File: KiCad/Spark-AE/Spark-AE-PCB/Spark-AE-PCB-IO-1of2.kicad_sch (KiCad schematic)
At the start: 21 parts, among them J3 Inputs, J4 Outputs, U4 MCP6002-xSN, U5 MCP6002-xSN

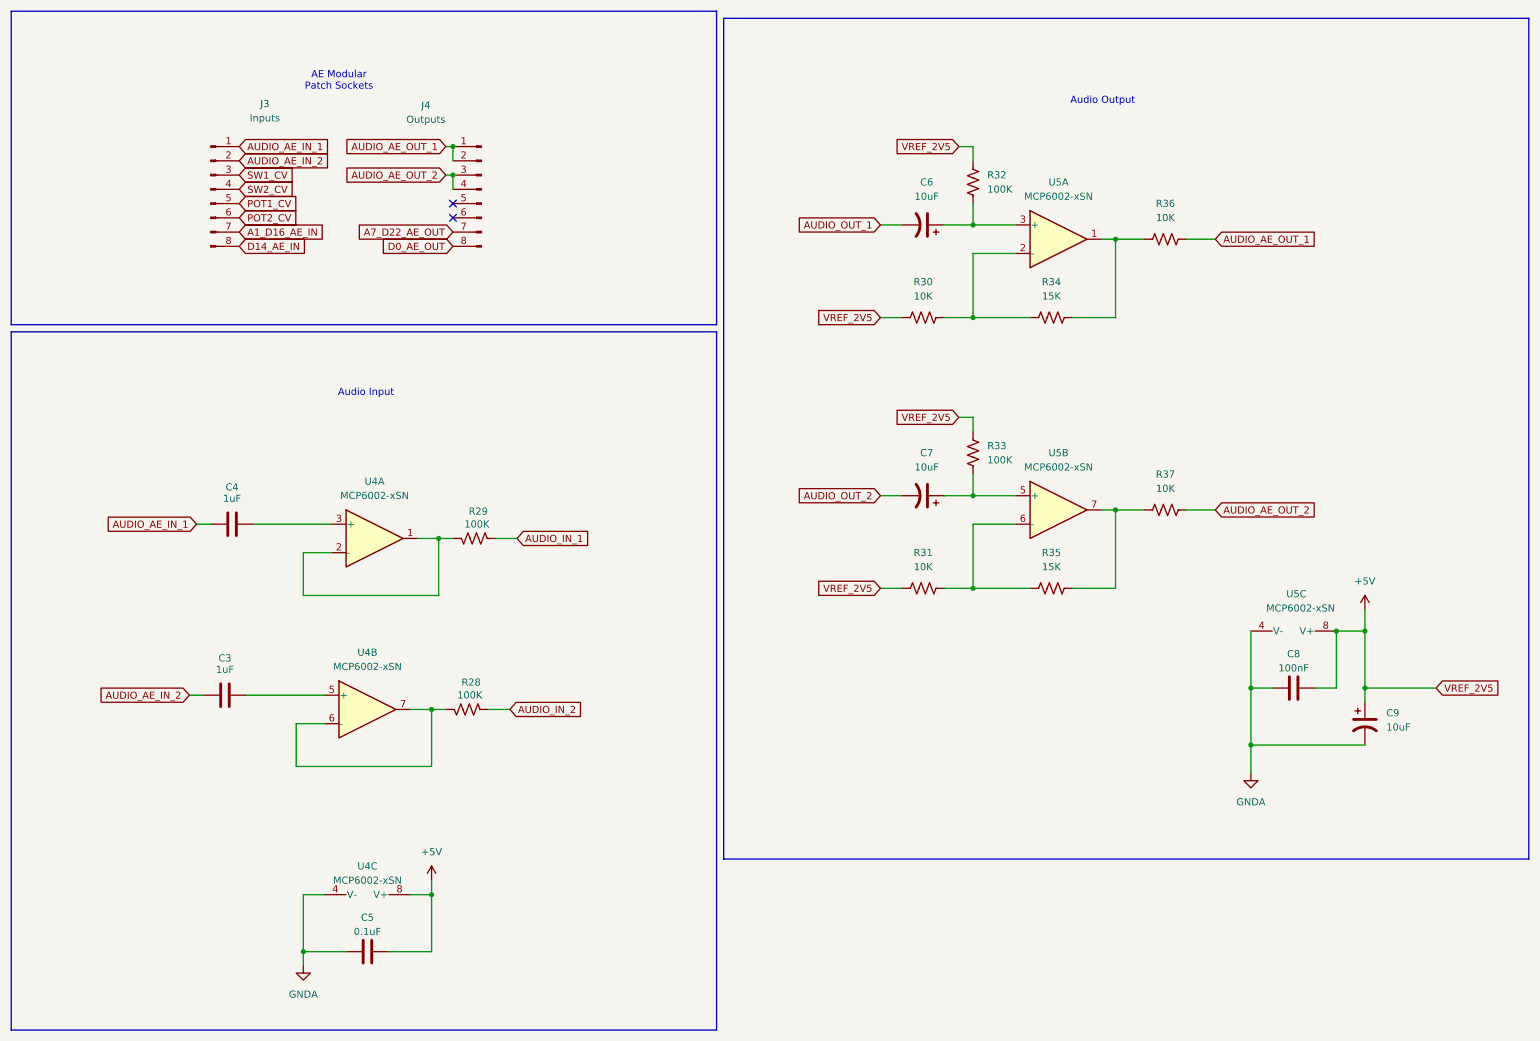
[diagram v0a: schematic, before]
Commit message: assigned footprints & sorted ratsnest
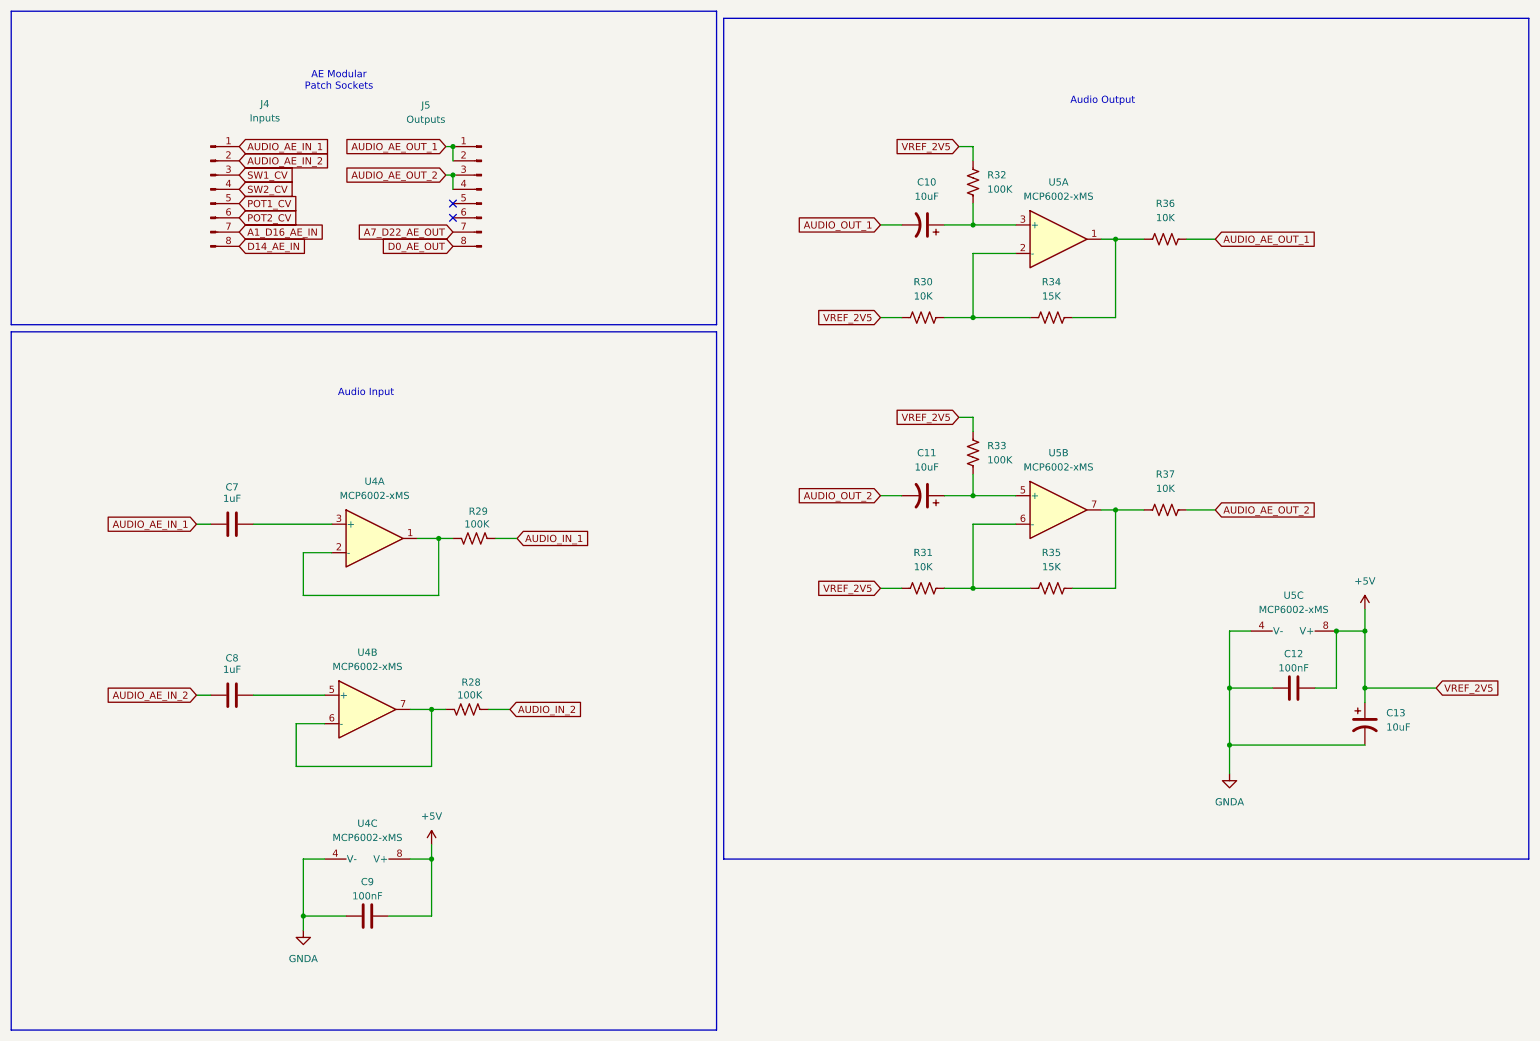
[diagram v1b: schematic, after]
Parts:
- removed U4, U5: MCP6002-xSN, symbol Amplifier_Operational:MCP6002-xSN
- added U4, U5: MCP6002-xMS, clectric-diy:Amplifier_Operational_Microchip_MCP6002T-I_MS, symbol Amplifier_Operational:MCP6002-xMS
- C10: renamed from C6; footprint (none) -> Capacitor_SMD:CP_Elec_4x5.4
- C11: renamed from C7; footprint (none) -> Capacitor_SMD:CP_Elec_4x5.4
- C12: renamed from C8; footprint (none) -> Capacitor_SMD:C_0603_1608Metric
- C13: renamed from C9; footprint (none) -> Capacitor_SMD:CP_Elec_4x5.4
- C7: renamed from C4; footprint Capacitor_THT:C_Rect_L7.2mm_W2.5mm_P5.00mm -> Capacitor_SMD:C_0603_1608Metric
- C8: renamed from C3; footprint Capacitor_THT:C_Rect_L7.2mm_W2.5mm_P5.00mm -> Capacitor_SMD:C_0603_1608Metric
- C9: renamed from C5; value 0.1uF -> 100nF; footprint (none) -> Capacitor_SMD:C_0603_1608Metric
- J4: renamed from J3; footprint (none) -> clectric-diy:Connector_PinSocket-1x08-P2.54mm-H8.5mm_Preci-Dip_801-87-008-10-005101
- J5: renamed from J4; footprint (none) -> clectric-diy:Connector_PinSocket-1x08-P2.54mm-H8.5mm_Preci-Dip_801-87-008-10-005101
- R28, R29, R30, R31, R32, R33, R34, R35, R36, R37: footprint (none) -> Resistor_SMD:R_0603_1608Metric
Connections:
- net +5V: now also U4.8 (V+), U5.8 (V+)
- net GNDA: now also U4.4 (V-), U5.4 (V-)
- net at R28.1: now also U4.6 (-), U4.7
- net at R29.1: now also U4.1, U4.2 (-)
- net at C7.2: now also U4.3 (+)
- net at R30.2, R34.1: now also U5.2 (-)
- net at R34.2, R36.1: now also U5.1
- net at R31.2, R35.1: now also U5.6 (-)
- net at R35.2, R37.1: now also U5.7
- net at C10.1, R32.2: now also U5.3 (+)
- net at C11.1, R33.2: now also U5.5 (+)
- net at C8.2: now also U4.5 (+)
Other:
- moved on the sheet: C8, C9

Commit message: schematic 100% complete. pcb layout around 50% complete.
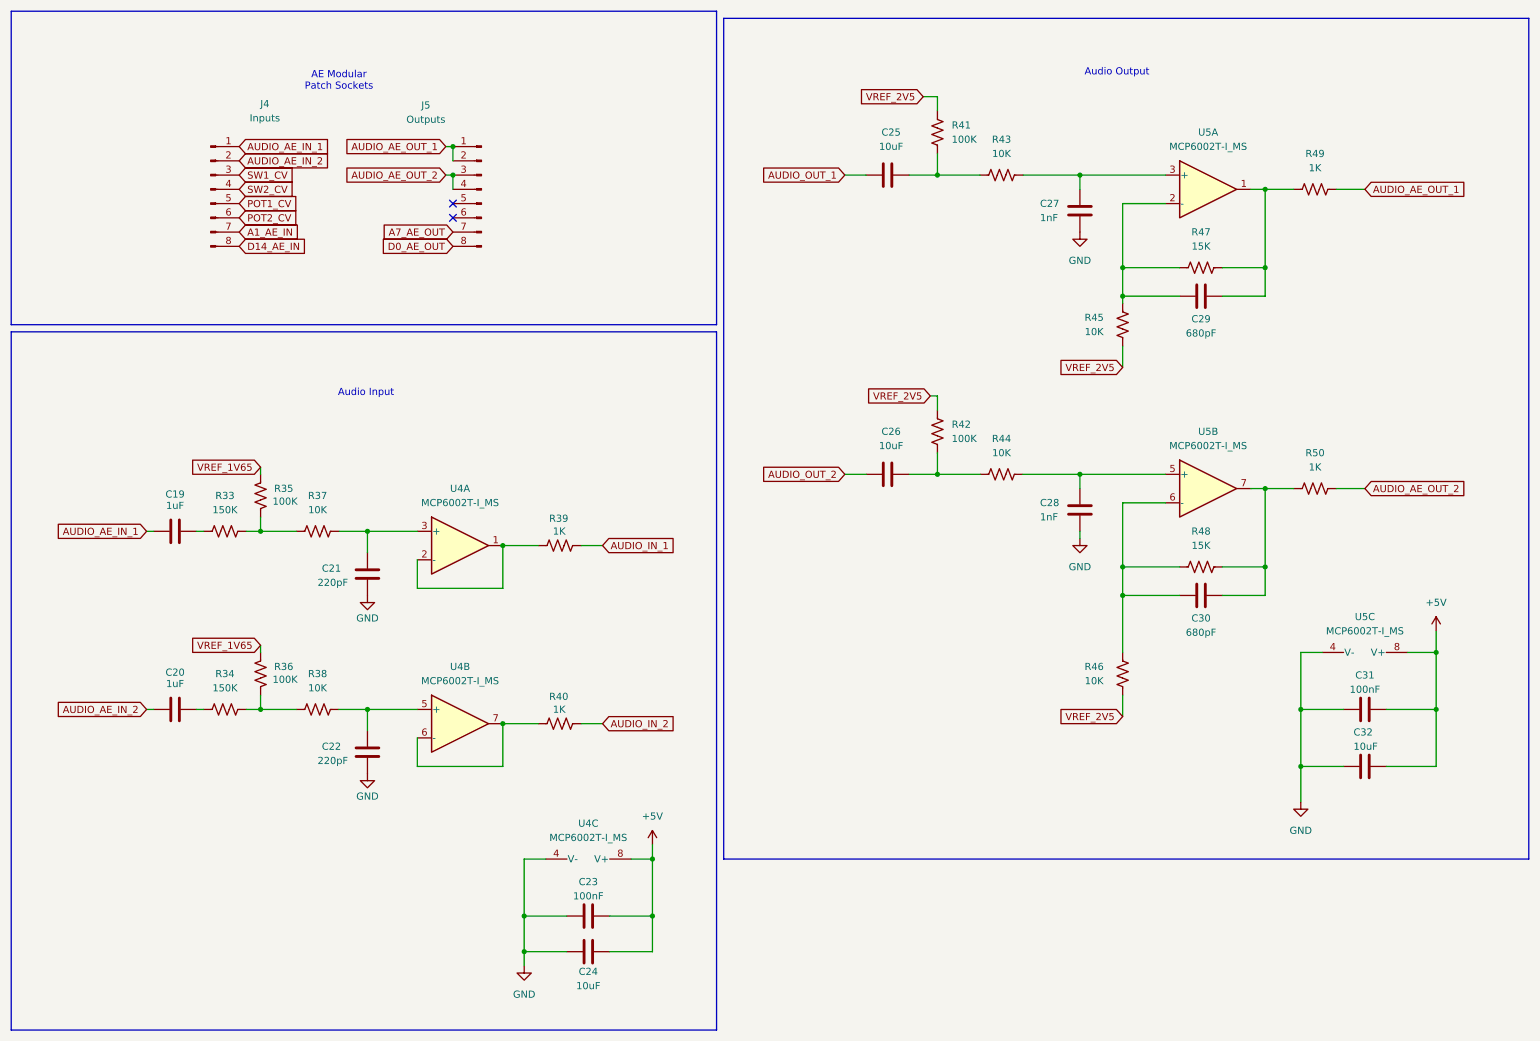
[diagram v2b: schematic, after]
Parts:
- removed C7: 1uF, Capacitor_SMD:C_0603_1608Metric, symbol Device:C
- removed R29: 100K, Resistor_SMD:R_0603_1608Metric, symbol Device:R_US
- added C19: 1uF, Capacitor_SMD:C_0603_1608Metric, symbol Device:C
- added C21, C22: 220pF, Capacitor_SMD:C_0603_1608Metric, symbol Device:C
- added C24: 10uF, Capacitor_SMD:C_0603_1608Metric, symbol Device:C
- added C27, C28: 1nF, Capacitor_SMD:C_0603_1608Metric, symbol Device:C
- added C29, C30: 680pF, Capacitor_SMD:C_0603_1608Metric, symbol Device:C
- added R33, R34: 150K, Resistor_SMD:R_0603_1608Metric, symbol Device:R_US
- added R35, R36: 100K, Resistor_SMD:R_0603_1608Metric, symbol Device:R_US
- added R37, R38, R43, R44: 10K, Resistor_SMD:R_0603_1608Metric, symbol Device:R_US
- added R39: 1K, Resistor_SMD:R_0603_1608Metric, symbol Device:R_US
- C25: renamed from C10; footprint Capacitor_SMD:CP_Elec_4x5.4 -> Capacitor_SMD:C_0603_1608Metric; symbol Device:C_Polarized_US -> Device:C
- C26: renamed from C11; footprint Capacitor_SMD:CP_Elec_4x5.4 -> Capacitor_SMD:C_0603_1608Metric; symbol Device:C_Polarized_US -> Device:C
- C32: renamed from C13; footprint Capacitor_SMD:CP_Elec_4x5.4 -> Capacitor_SMD:C_0603_1608Metric; symbol Device:C_Polarized_US -> Device:C
- R40: renamed from R28; value 100K -> 1K
- R49: renamed from R36; value 10K -> 1K
- R50: renamed from R37; value 10K -> 1K
- U4, U5: value MCP6002-xMS -> MCP6002T-I_MS
- renumbered C8 to C20, C9 to C23, C12 to C31, R32 to R41, R33 to R42, R30 to R45, R31 to R46, R34 to R47, R35 to R48
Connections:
- net +5V: now also C24.2; no longer R41.1, R42.1, R45.1, R46.1
- net AUDIO_AE_IN_1: now also C19.1
- net AUDIO_IN_1: now also R39.1
- net AUDIO_IN_2: now also R40.1; no longer R40.2
- net at U4.6 (-), U4.7: now also R40.2; no longer R40.1
- net at C26.1, R42.2: now also R44.1; no longer U5.5 (+)
- net at R46.2, R48.1, U5.6 (-): now also C30.2
- net at R48.2, R50.1, U5.7: now also C30.1
- net at U4.5 (+): now also C22.1, R38.2; no longer C20.2
- net at R45.2, R47.1, U5.2 (-): now also C29.2
- net at R47.2, R49.1, U5.1: now also C29.1
- net at C25.1, R41.2: now also R43.1; no longer U5.3 (+)
- net at U4.3 (+): now also C21.1, R37.2
- net at U4.1, U4.2 (-): now also R39.2
- net A1_D16_AE_IN renamed A1_AE_IN
- net A7_D22_AE_OUT renamed A7_AE_OUT
- net GNDA renamed GND
- net GND: now also C21.2, C22.2, C24.1, C27.2, C28.2
- new net: R33.2, R35.1, R37.1
- new net: C19.2, R33.1
- new net: C27.1, R43.2, U5.3 (+)
- new net: R34.2, R36.1, R38.1
- new net: C28.1, R44.2, U5.5 (+)
- new net: C20.2, R34.1
- new net VREF_1V65: R35.2, R36.2
- new net VREF_2V5: R41.1, R42.1, R45.1, R46.1
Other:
- moved on the sheet: C20, C23, C31, R40, R41, R42, R45, R46, R47, R48, R49, R50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

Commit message: continuing to plug away at pcb layout
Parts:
- renumbered C19 to C17, C20 to C18, C21 to C19, C22 to C20, C23 to C21, C24 to C22, C25 to C23, C26 to C24, C27 to C25, C28 to C26, C29 to C27, C30 to C28, C31 to C29, C32 to C30
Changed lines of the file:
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@@
 	(wire
 		(pts
-			(xy 86.36 148.59) (xy 86.36 143.51)
+			(xy 86.36 143.51) (xy 86.36 148.59)
 		)
 		(stroke
@@
 	(wire
 		(pts
-			(xy 267.97 124.46) (xy 267.97 128.27)
+			(xy 101.6 140.97) (xy 101.6 148.59)
 		)
 		(stroke
@@
 	(wire
 		(pts
-			(xy 267.97 128.27) (xy 267.97 138.43)
+			(xy 267.97 124.46) (xy 267.97 128.27)
 		)
 		(stroke
@@
 	(wire
 		(pts
-			(xy 179.07 92.71) (xy 179.07 96.52)
+			(xy 267.97 128.27) (xy 267.97 138.43)
 		)
 		(stroke
@@
 	(wire
 		(pts
-			(xy 101.6 140.97) (xy 101.6 148.59)
+			(xy 179.07 92.71) (xy 179.07 96.52)
 		)
 		(stroke
@@
 		(on_board yes)
 		(dnp no)
-		(property "Reference" "C19"
+		(property "Reference" "C17"
 			(at 43.18 100.076 90)
 			(effects
@@
 			(project "Spark-AE-PCB"
 				(path "/b249adcd-2848-4e56-9615-c4f1b6083abe/83b47d21-ef52-416e-8f7d-192d4edc9907"
-					(reference "C19")
+					(reference "C17")
 					(unit 1)
 				)
@@
 		(on_board yes)
 		(dnp no)
-		(property "Reference" "C24"
+		(property "Reference" "C22"
 			(at 116.84 185.166 90)
 			(effects
@@
 			(project "Spark-AE-PCB"
 				(path "/b249adcd-2848-4e56-9615-c4f1b6083abe/83b47d21-ef52-416e-8f7d-192d4edc9907"
-					(reference "C24")
+					(reference "C22")
 					(unit 1)
 				)
@@
 		(on_board yes)
 		(dnp no)
-		(property "Reference" "C32"
+		(property "Reference" "C30"
 			(at 253.238 142.494 90)
 			(effects
@@
 			(project "Spark-AE-PCB"
 				(path "/b249adcd-2848-4e56-9615-c4f1b6083abe/83b47d21-ef52-416e-8f7d-192d4edc9907"
-					(reference "C32")
+					(reference "C30")
 					(unit 1)
 				)
@@
 		(on_board yes)
 		(dnp no)
-		(property "Reference" "C28"
+		(property "Reference" "C26"
 			(at 197.358 101.6 0)
 			(effects
@@
 			(project "Spark-AE-PCB"
 				(path "/b249adcd-2848-4e56-9615-c4f1b6083abe/83b47d21-ef52-416e-8f7d-192d4edc9907"
-					(reference "C28")
+					(reference "C26")
 					(unit 1)
 				)
@@
 		(on_board yes)
 		(dnp no)
-		(property "Reference" "C29"
+		(property "Reference" "C27"
 			(at 226.06 68.834 90)
 			(effects
@@
 			(project ""
 				(path "/b249adcd-2848-4e56-9615-c4f1b6083abe/83b47d21-ef52-416e-8f7d-192d4edc9907"
-					(reference "C29")
+					(reference "C27")
 					(unit 1)
 				)
@@
 		(on_board yes)
 		(dnp no)
-		(property "Reference" "C21"
+		(property "Reference" "C19"
 			(at 69.342 113.284 0)
 			(effects
@@
 			(project "Spark-AE-PCB"
 				(path "/b249adcd-2848-4e56-9615-c4f1b6083abe/83b47d21-ef52-416e-8f7d-192d4edc9907"
-					(reference "C21")
+					(reference "C19")
 					(unit 1)
 				)
@@
 		(on_board yes)
 		(dnp no)
-		(property "Reference" "C25"
+		(property "Reference" "C23"
 			(at 170.815 35.56 90)
 			(effects
@@
 			(project "Spark-AE-PCB"
 				(path "/b249adcd-2848-4e56-9615-c4f1b6083abe/83b47d21-ef52-416e-8f7d-192d4edc9907"
-					(reference "C25")
+					(reference "C23")
 					(unit 1)
 				)
@@
 		(on_board yes)
 		(dnp no)
-		(property "Reference" "C20"
+		(property "Reference" "C18"
 			(at 43.18 131.826 90)
 			(effects
@@
 			(project "Spark-AE-PCB"
 				(path "/b249adcd-2848-4e56-9615-c4f1b6083abe/83b47d21-ef52-416e-8f7d-192d4edc9907"
-					(reference "C20")
+					(reference "C18")
 					(unit 1)
 				)
@@
 		(on_board yes)
 		(dnp no)
-		(property "Reference" "C26"
+		(property "Reference" "C24"
 			(at 170.815 88.9 90)
 			(effects
@@
 			(project "Spark-AE-PCB"
 				(path "/b249adcd-2848-4e56-9615-c4f1b6083abe/83b47d21-ef52-416e-8f7d-192d4edc9907"
-					(reference "C26")
+					(reference "C24")
 					(unit 1)
 				)
@@
 		(on_board yes)
 		(dnp no)
-		(property "Reference" "C27"
+		(property "Reference" "C25"
 			(at 197.358 48.26 0)
 			(effects
@@
 			(project "Spark-AE-PCB"
 				(path "/b249adcd-2848-4e56-9615-c4f1b6083abe/83b47d21-ef52-416e-8f7d-192d4edc9907"
-					(reference "C27")
+					(reference "C25")
 					(unit 1)
 				)
@@
 		(on_board yes)
 		(dnp no)
-		(property "Reference" "C31"
+		(property "Reference" "C29"
 			(at 255.27 132.334 90)
 			(effects
@@
 			(project "Spark-AE-PCB"
 				(path "/b249adcd-2848-4e56-9615-c4f1b6083abe/83b47d21-ef52-416e-8f7d-192d4edc9907"
-					(reference "C31")
+					(reference "C29")
 					(unit 1)
 				)
@@
 		(on_board yes)
 		(dnp no)
-		(property "Reference" "C22"
+		(property "Reference" "C20"
 			(at 69.342 145.034 0)
 			(effects
@@
 			(project ""
 				(path "/b249adcd-2848-4e56-9615-c4f1b6083abe/83b47d21-ef52-416e-8f7d-192d4edc9907"
-					(reference "C22")
+					(reference "C20")
 					(unit 1)
 				)
@@
 		(on_board yes)
 		(dnp no)
-		(property "Reference" "C23"
+		(property "Reference" "C21"
 			(at 116.84 169.164 90)
 			(effects
@@
 			(project "Spark-AE-PCB"
 				(path "/b249adcd-2848-4e56-9615-c4f1b6083abe/83b47d21-ef52-416e-8f7d-192d4edc9907"
-					(reference "C23")
+					(reference "C21")
 					(unit 1)
 				)
@@
 		(on_board yes)
 		(dnp no)
-		(property "Reference" "C30"
+		(property "Reference" "C28"
 			(at 226.06 122.174 90)
 			(effects
@@
 			(project ""
 				(path "/b249adcd-2848-4e56-9615-c4f1b6083abe/83b47d21-ef52-416e-8f7d-192d4edc9907"
-					(reference "C30")
+					(reference "C28")
 					(unit 1)
 				)
